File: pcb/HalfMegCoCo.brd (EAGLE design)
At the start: 73.7 x 68.6 mm, 10 parts, among them IC1 44256, IC2 44256, IC3 44256, IC4 44256, X1 COCO3_RAM_EXPANSION-RP

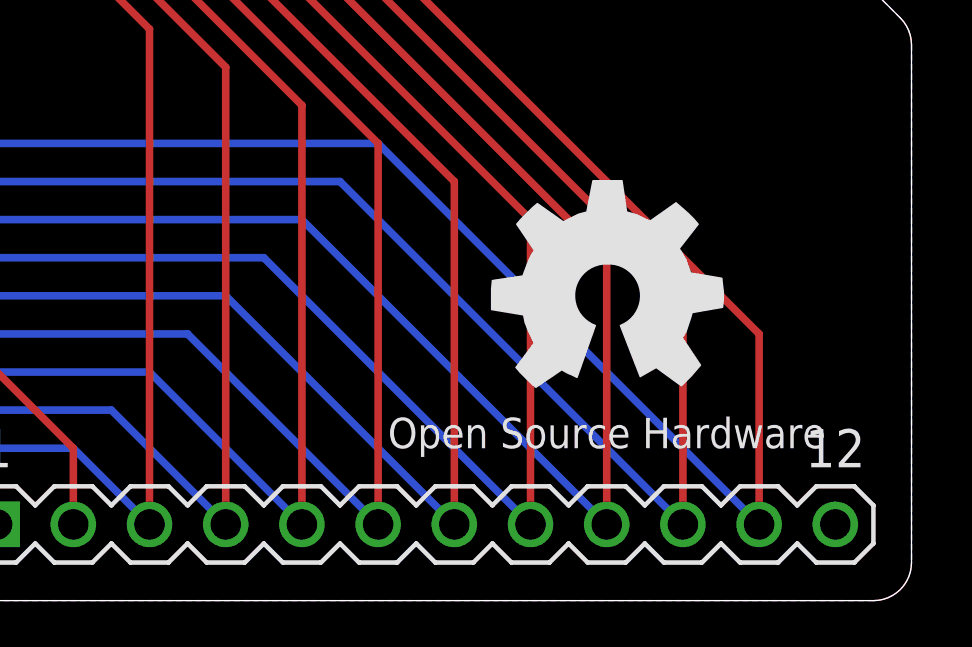
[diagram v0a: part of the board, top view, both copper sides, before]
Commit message: Fixed filename
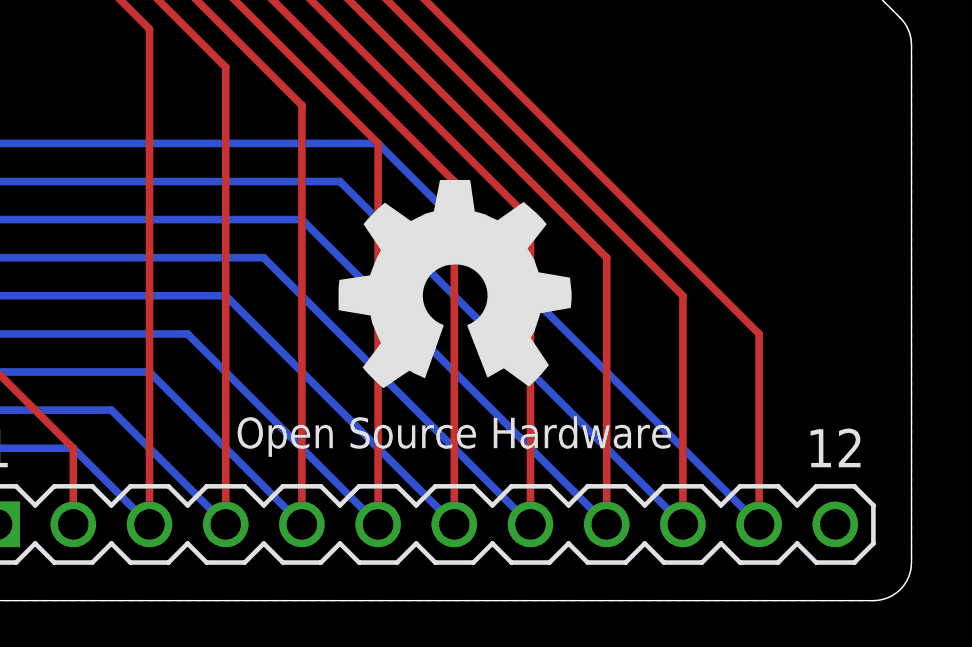
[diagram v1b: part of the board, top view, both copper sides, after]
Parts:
- moved GOLD_ORB_SM1 5.08 mm to (-40.6, 21.6)
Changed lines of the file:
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@@
 <rectangle x1="-47.6631" y1="35.613340625" x2="-47.4954625" y2="35.618415625" layer="200"/>
 <rectangle x1="-61.998859375" y1="35.61841875" x2="-61.866784375" y2="35.6235" layer="200"/>
+<dimension x1="-97.79" y1="80.01" x2="-97.79" y2="11.43" x3="-100.33" y3="45.72" textsize="1.778" layer="48"/>
+<dimension x1="-99.06" y1="12.7" x2="-25.4" y2="12.7" x3="-62.23" y3="7.62" textsize="1.778" layer="48"/>
 </plain>
 <attributes>
@@
 <element name="C3" library="rcl" package="C050-025X075" value="" x="-85.09" y="13.335"/>
 <element name="C4" library="rcl" package="C050-025X075" value="" x="-72.39" y="13.335"/>
-<element name="GOLD_ORB_SM1" library="oshw" package="OSHW_8MM" value="Open Source Hardware" x="-35.56" y="21.59"/>
+<element name="GOLD_ORB_SM1" library="oshw" package="OSHW_8MM" value="Open Source Hardware" x="-40.64" y="21.59"/>
 <element name="X1" library="coco" package="RAM_EXPANSION-RP" value="COCO3_RAM_EXPANSION-RP" x="-62.23" y="45.72" smashed="yes">
 <attribute name="NAME" x="-97.79" y="15.24" size="1.27" layer="25" ratio="10"/>

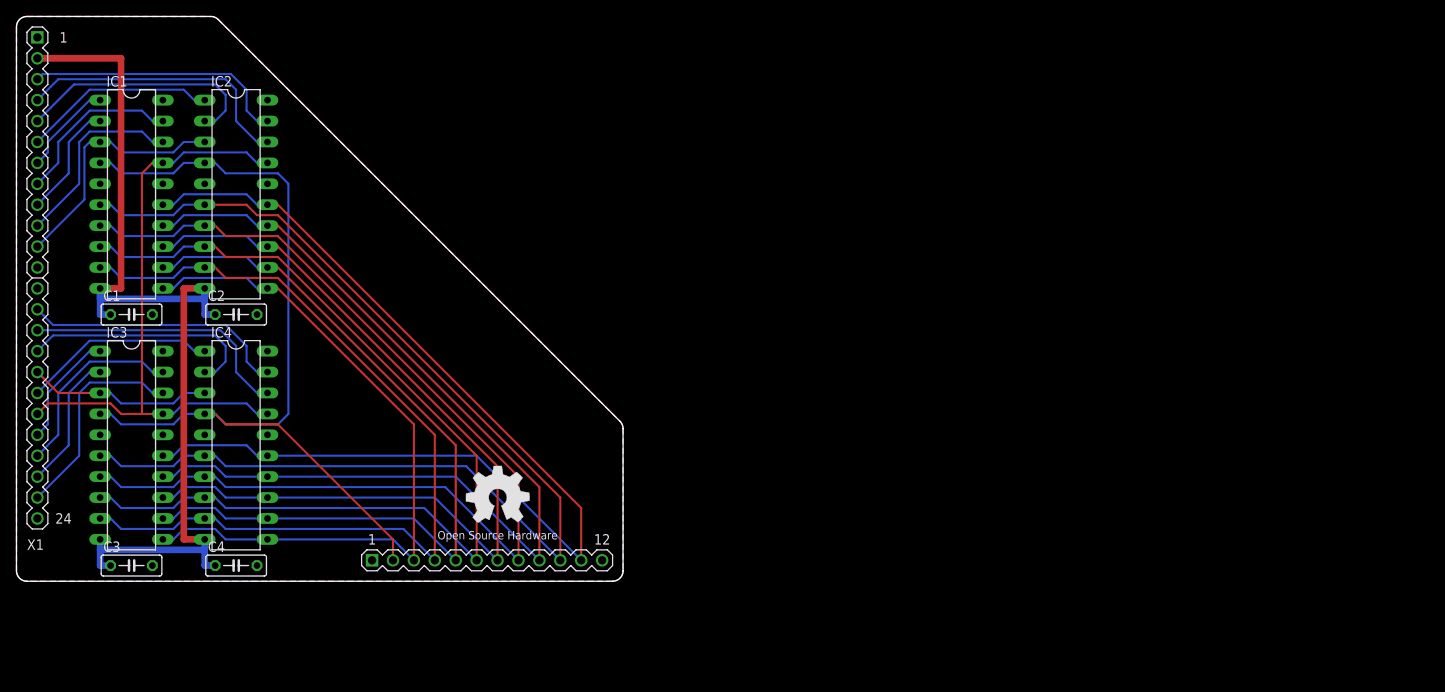
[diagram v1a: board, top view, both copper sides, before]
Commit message: SRAM-based version added, DRAM version removed.
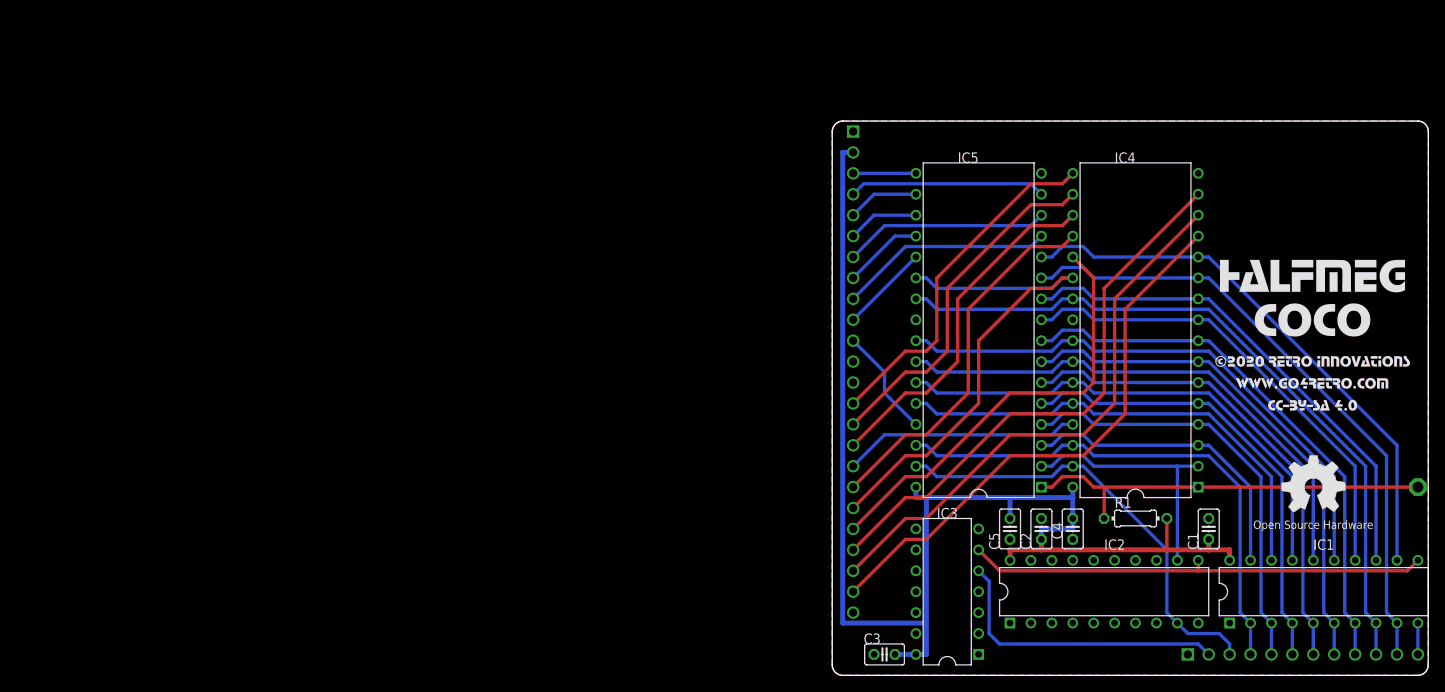
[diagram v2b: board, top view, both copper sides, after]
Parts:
- removed X1: COCO3_RAM_EXPANSION-RP, coco:RAM_EXPANSION-RP
- added BANK0: PTR1PAD1-13, testpad:P1-13
- added C5: .1, rcl:C025-025X050
- added CN1: COCO3_RAM_EXPANSION-RRP, coco:RAM_EXPANSION_REV_RP
- added IC5: AS6C4008PCNR, memory-alliance:DIL32-RP
- added R1: 10K, resistor:0204/7
- C1, C2, C3, C4: value (none) -> .1; device rcl:C050-025X075 -> rcl:C025-025X050
- IC1, IC2: value 44256 -> 74ABT574N; device memory-jlb:DIL20 -> 74xx-us-jlb:DIL20-RP
- IC3: value 44256 -> 74ABT04N; device memory-jlb:DIL20 -> 74xx-us-jlb:DIL14-RP
- IC4: value 44256 -> AS6C4008PCNR; device memory-jlb:DIL20 -> memory-alliance:DIL32-RP
- moved IC1 152.6 mm to (59.7, 10.2), turned to 0 degrees
- moved C1 133.4 mm to (45.7, 17.8), turned to 90 degrees
- moved IC2 115.9 mm to (33.0, 10.2), turned to 0 degrees
- moved IC4 110.1 mm to (36.8, 41.9), turned to 90 degrees
- moved C4 101.7 mm to (29.2, 17.8), turned to 270 degrees
- moved C2 101.2 mm to (25.4, 17.8), turned to 90 degrees
- moved IC3 100.6 mm to (14.0, 10.2), turned to 90 degrees
- moved GOLD_ORB_SM1 99.1 mm to (58.4, 22.9)
- moved C3 92.1 mm to (6.35, 2.54), turned to 180 degrees
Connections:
- new net BANK0: BANK0.TP, IC4.1, IC5.1, R1.1
- new net MA0: CN1.B3, IC2.9, IC4.31, IC5.31
- new net MA1: CN1.B4, IC1.2, IC4.30, IC5.30
- new net MA2: CN1.B5, IC1.3, IC4.4, IC5.4
- new net MA3: CN1.B6, IC1.4, IC4.5, IC5.5
- new net MA4: CN1.B9, IC1.7, IC4.8, IC5.8
- new net MA5: CN1.B8, IC1.6, IC4.7, IC5.7
- new net MA6: CN1.B7, IC1.5, IC4.6, IC5.6
- new net MA7: CN1.B10, IC1.8, IC4.23, IC5.23
- new net MA8: CN1.B11, IC1.9, IC4.11, IC5.11
- new net N$6: IC1.11, IC2.11, IC3.6
- net !CAS: now also CN1.A19, IC4.22, IC5.22; no longer IC1.17, IC2.17, IC3.17, IC4.17, X1.A19
- net !RAS: now also CN1.B2, IC3.5; no longer IC1.4, IC2.4, IC3.4, IC4.4, X1.B2
- net !WE0: now also CN1.A17, IC4.29; no longer IC3.3, IC4.3, X1.A17
- net !WE1: now also CN1.A11, IC5.29; no longer IC1.3, IC2.3, X1.A11
- net A0: now also IC2.12, IC4.2, IC5.2; no longer IC1.11, IC2.11, IC3.11, IC4.11, X1.B3
- net A1: now also IC1.19, IC4.3, IC5.3; no longer IC1.9, IC2.9, IC3.9, IC4.9, X1.B4
- net A2: now also IC1.18, IC4.28, IC5.28; no longer IC1.12, IC2.12, IC3.12, IC4.12, X1.B5
- net A3: now also IC1.17, IC4.27, IC5.27; no longer IC1.8, IC2.8, IC3.8, IC4.8, X1.B6
- net A4: now also IC4.9, IC5.9; no longer IC2.14, IC3.14, IC4.14, X1.B9
- net A5: now also IC1.15, IC4.25, IC5.25; no longer IC1.7, IC2.7, IC3.7, IC4.7, X1.B8
- net A6: now also IC1.16, IC4.26, IC5.26; no longer IC1.13, IC2.13, IC3.13, IC4.13, X1.B7
- net A7: now also IC1.13, IC4.10, IC5.10; no longer IC1.6, IC2.6, IC3.6, IC4.6, X1.B10
- net A8: now also IC1.12, IC4.12, IC5.12; no longer IC1.15, IC2.15, IC3.15, IC4.15, X1.B11
- net D0: now also CN1.A18, IC4.20; no longer IC4.1, X1.A18
- net D1: now also CN1.A16, IC4.19; no longer IC4.2, X1.A16
- net D10: now also CN1.A5, IC5.18; no longer IC2.2, X1.A5
- net D11: now also CN1.A6, IC5.19; no longer IC2.1, X1.A6
- net D12: now also CN1.A10, IC5.21; no longer IC1.18, X1.A10
- net D13: now also CN1.A9, IC5.13; no longer IC1.2, X1.A9
- net D14: now also CN1.A7, IC5.14; no longer IC1.1, X1.A7
- net D15: now also CN1.A8, IC5.20; no longer IC1.19, X1.A8
- net D2: now also CN1.A14, IC4.17; no longer IC4.19, X1.A14
- net D3: now also CN1.A15; no longer X1.A15
- net D4: now also CN1.A22, IC4.14; no longer IC3.2, X1.A22
- net D5: now also CN1.A21, IC4.15; no longer IC3.19, X1.A21
- net D6: now also CN1.A23, IC4.13; no longer IC3.18, X1.A23
- net D7: now also CN1.A20, IC4.21; no longer IC3.1, X1.A20
- net D8: now also CN1.A4, IC5.15; no longer IC2.18, X1.A4
- net D9: now also CN1.A3, IC5.17; no longer IC2.19, X1.A3
- net GND: now also C5.2, CN1.A1, CN1.A12, CN1.A13, CN1.A24, CN1.B1, CN1.B12, IC1.1, IC1.10, IC2.1, IC2.10, IC2.2, IC2.3, IC2.4, IC2.5, IC2.6, IC2.7, IC2.8, IC3.1, IC3.11, IC3.13, IC3.3, IC3.7, IC3.9, IC4.24, IC5.16, IC5.24; no longer IC1.16, IC1.20, IC2.16, IC2.20, IC3.16, IC3.20, IC4.20, X1.A1, X1.A12, X1.A13, X1.A24, X1.B1, X1.B12
- net VCC: now also C5.1, CN1.A2, IC1.20, IC2.20, IC3.14, IC4.32, IC5.32, R1.2; no longer IC1.10, IC2.10, IC3.10, IC4.10, X1.A2
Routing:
- net MA7: track 0.00 -> 87.5 mm
- net A7: track 141.5 -> 61.5 mm
- net MA8: track 0.00 -> 76.6 mm
- net !RAS: track 109.6 -> 35.9 mm
- net A1: track 109.1 -> 37.4 mm
- net MA4: track 0.00 -> 66.8 mm
- net MA1: track 0.00 -> 63.4 mm
- net MA5: track 0.00 -> 63.2 mm
- net A8: track 130.6 -> 67.7 mm
- net A5: track 130.7 -> 68.9 mm
- net A4: track 119.8 -> 57.9 mm
- net MA6: track 0.00 -> 59.7 mm
- net A3: track 119.9 -> 61.7 mm
- net N$6: track 0.00 -> 56.2 mm
- net MA3: track 0.00 -> 56.1 mm
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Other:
- board size 73.7 x 68.6 mm -> 72.4 x 67.3 mm
